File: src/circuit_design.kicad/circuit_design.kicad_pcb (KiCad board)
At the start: 2 copper layers, 198.8 x 170.8 mm, 186 parts, among them J1 CONN_BAT, Q1 BT134-600E, Q2 BT134-600E, Q3 BT134-600E, Q4 BT134-600E, U1 К176ИЕ12, U10 К155ЛА4, U11 К155ЛИ1, U12 К155ЛА1, U13 К155ИЕ5, U14 К155ЛЛ1, U15 К155ЛН1, U16 К155ЛИ1, U17 К155ТВ15, U18 К155ИЕ5, U19 К155ЛП5, U2 К155ЛП10, U20 К155ИВ1, U21 К155ИД7, U22 К155ИД4, U23 К155ЛН1, U24 К155ЛП10, U25 MOC3062M, U26 MOC3062M, U27 MOC3062M, U28 MOC3062M, U29 LM7806_TO220, U3 К155ЛЕ3, U30 SC6038, U31 К155ЛЕ1, U32 К155ЛН1, U33 К155ЛИ1, U34 К155ЛА4, U35 К155ТВ15, U36 К155ТЛ2, U37 4020, U38 LM7806_TO220, U39 К155ЛН1, U4 К155ЛН1, U5 К155ЛИ1, U6 К155ЛЛ1, U7 4020, U8 ICL7660, U9 К155ИЕ5, Y1 32768

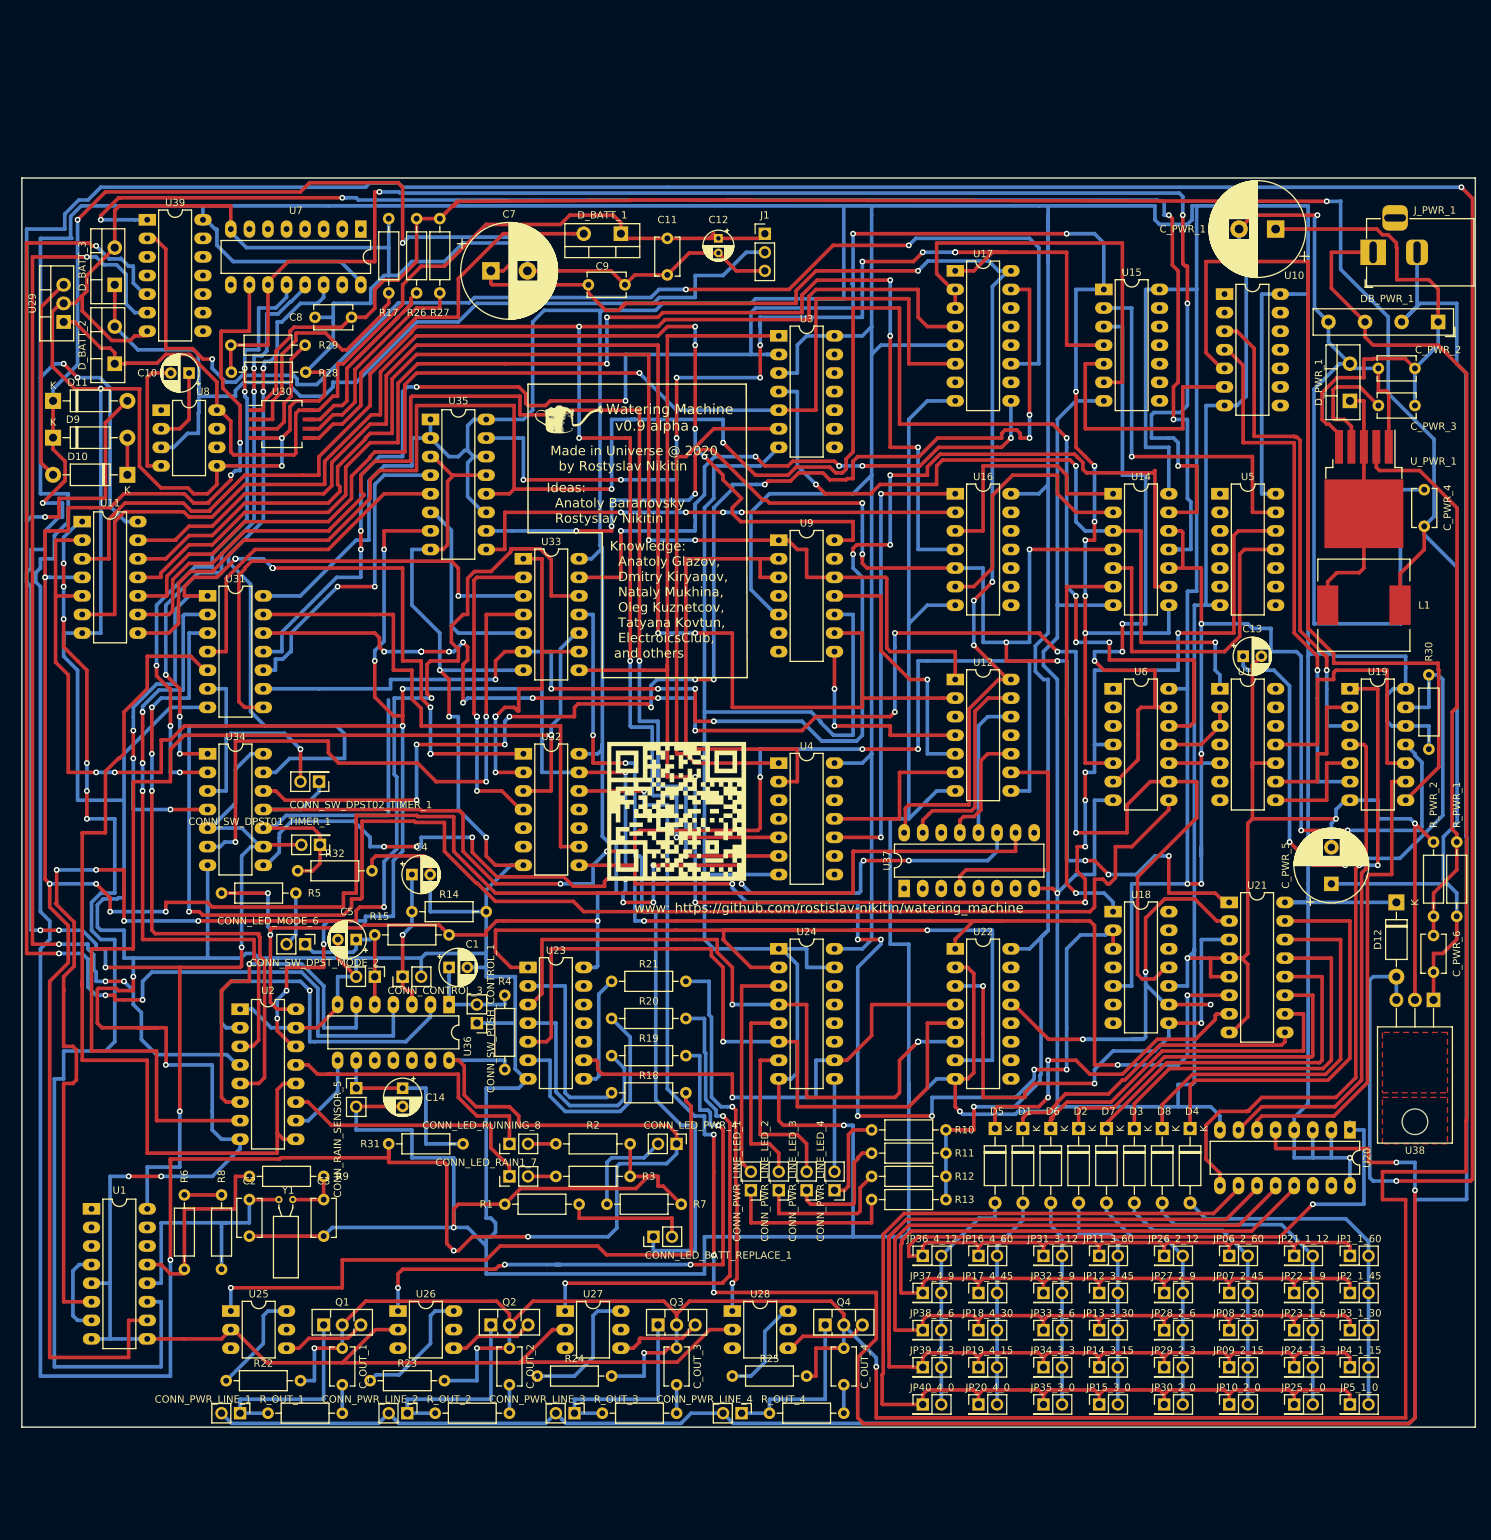
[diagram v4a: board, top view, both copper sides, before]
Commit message: 01. The power module was moved bottom 02. The zone time select jumpers was replaced with sliding switches 03. The zone time select module was moved top 04. The 24-hour timer LED circuit was added
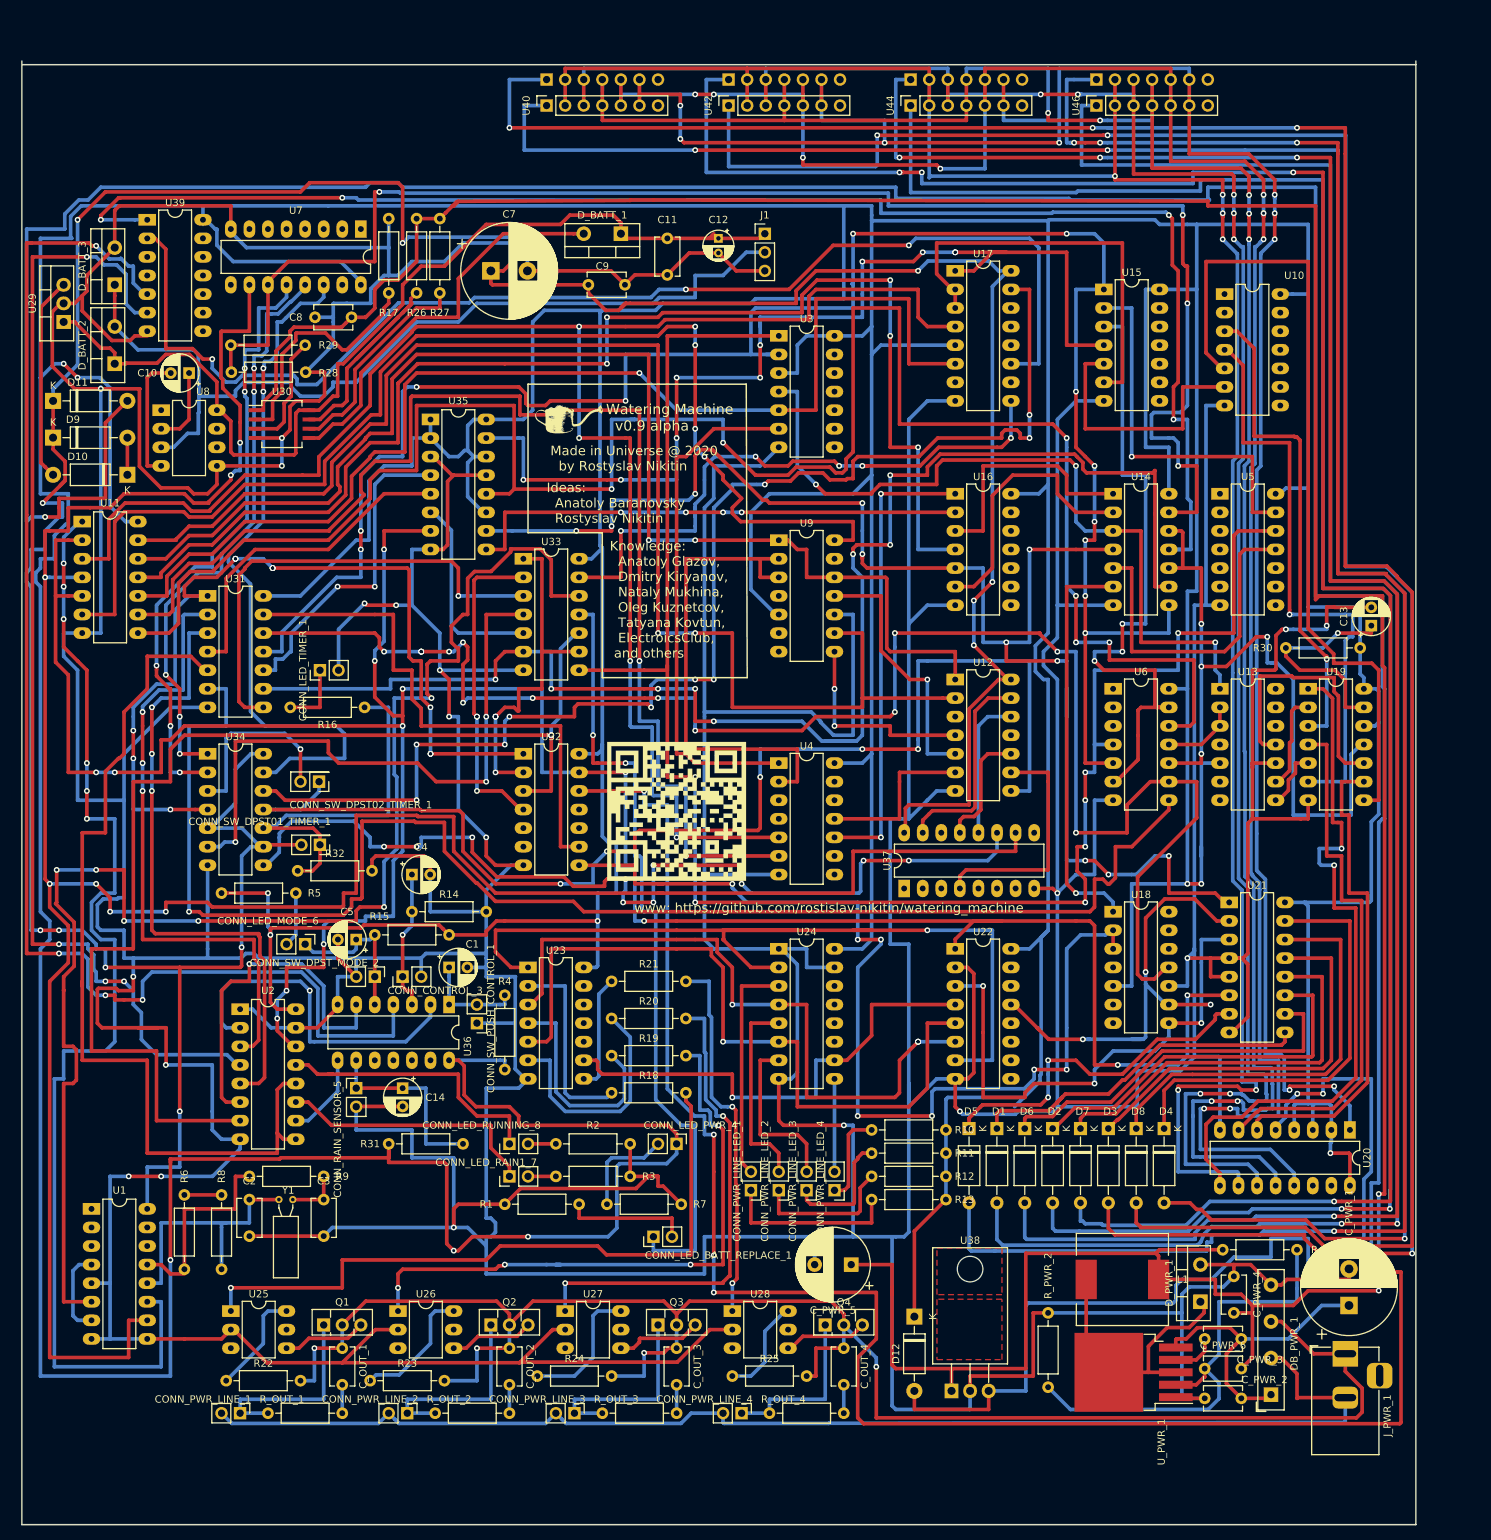
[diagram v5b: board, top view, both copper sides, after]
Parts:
- removed JP06_2_60, JP07_2_45, JP08_2_30, JP09_2_15, JP10_2_0, JP11_3_60, JP12_3_45, JP13_3_30, JP14_3_15, JP15_3_0, JP16_4_60, JP17_4_45, JP18_4_30, JP19_4_15, JP1_1_60, JP20_4_0, JP21_1_12, JP22_1_9, JP23_1_6, JP24_1_3, JP25_1_0, JP26_2_12, JP27_2_9, JP28_2_6, JP29_2_3, JP2_1_45, JP30_2_0, JP31_3_12, JP32_3_9, JP33_3_6, JP34_3_3, JP35_3_0, JP36_4_12, JP37_4_9, JP38_4_6, JP39_4_3, JP3_1_30, JP40_4_0, JP4_1_15, JP5_1_0: JP, Connector_PinHeader_2.54mm:PinHeader_2x01_P2.54mm_Vertical
- added CONN_LED_TIMER_1: Conn_01x02_Male, Connector_PinHeader_2.54mm:PinHeader_1x02_P2.54mm_Vertical, F.Cu at (90.9, 76.2)
- added R16: 270, Resistor_THT:R_Axial_DIN0207_L6.3mm_D2.5mm_P10.16mm_Horizontal, F.Cu at (97.0, 81.3)
- added U40: SPFT_Sliding_Switch, Connector_PinSocket_2.54mm:PinSocket_1x07_P2.54mm_Vertical, F.Cu at (121.9, -1.02)
- added U41: SPFT_Sliding_Switch, Connector_PinSocket_2.54mm:PinSocket_1x07_P2.54mm_Vertical, B.Cu at (121.9, -4.57)
- added U42: SPFT_Sliding_Switch, Connector_PinSocket_2.54mm:PinSocket_1x07_P2.54mm_Vertical, F.Cu at (146.8, -1.02)
- added U43: SPFT_Sliding_Switch, Connector_PinSocket_2.54mm:PinSocket_1x07_P2.54mm_Vertical, B.Cu at (146.8, -4.57)
- added U44: SPFT_Sliding_Switch, Connector_PinSocket_2.54mm:PinSocket_1x07_P2.54mm_Vertical, F.Cu at (171.7, -1.02)
- added U45: SPFT_Sliding_Switch, Connector_PinSocket_2.54mm:PinSocket_1x07_P2.54mm_Vertical, B.Cu at (171.7, -4.57)
- added U46: SPFT_Sliding_Switch, Connector_PinSocket_2.54mm:PinSocket_1x07_P2.54mm_Vertical, F.Cu at (197.1, -1.02)
- added U47: SPFT_Sliding_Switch, Connector_PinSocket_2.54mm:PinSocket_1x07_P2.54mm_Vertical, B.Cu at (197.1, -4.57)
- moved J_PWR_1 150.7 mm to (231.1, 169.7), turned to 90 degrees
- moved DB_PWR_1 148.5 mm to (221.0, 175.3), turned to 90 degrees
- moved C_PWR_1 147.5 mm to (231.6, 163.1), turned to 90 degrees
- moved C_PWR_2 142.8 mm to (216.9, 175.8)
- moved C_PWR_3 129.8 mm to (216.9, 167.6)
- moved D_PWR_1 124.9 mm to (211.3, 162.6)
- moved U_PWR_1 124.8 mm to (202.2, 172.2), turned to 180 degrees
- moved C_PWR_4 110.7 mm to (215.9, 164.1)
- moved L1 97.9 mm to (200.7, 159.5)
- moved D12 86.9 mm to (172.2, 164.6)
- moved U38 84.9 mm to (177.3, 174.8), turned to 0 degrees
- moved C_PWR_5 83.8 mm to (163.6, 157.5), turned to 180 degrees
- moved R_PWR_2 83.2 mm to (190.5, 174.2)
- moved C_PWR_6 60.3 mm to (216.9, 171.7), turned to 180 degrees
- moved R_PWR_1 55.7 mm to (214.4, 155.4), turned to 0 degrees
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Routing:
- net Net-(D8-Pad2): track 44.7 -> 328.3 mm, vias 0 -> 3
- net Net-(D7-Pad2): track 34.5 -> 299.9 mm, vias 0 -> 4
- net Net-(D3-Pad2): track 39.6 -> 303.5 mm, vias 0 -> 3
- net Net-(D4-Pad2): track 48.9 -> 311.7 mm, vias 0 -> 3
- net Net-(D6-Pad2): track 28.2 -> 282.6 mm, vias 0 -> 4
- net Net-(D5-Pad2): track 31.9 -> 275.7 mm, vias 0 -> 4
- net Net-(D2-Pad2): track 32.3 -> 270.3 mm, vias 0 -> 2
- net Net-(D1-Pad2): track 29.0 -> 258.6 mm, vias 0 -> 2
- net VAC: track 415.7 -> 238.4 mm
- net GNDREF: track 346.5 -> 176.3 mm
- net /D3: track 140.1 -> 301.8 mm, vias 0 -> 9
- net /D2: track 144.4 -> 295.7 mm, vias 0 -> 7
- net /D4: track 153.4 -> 296.6 mm, vias 1 -> 9
- net +9V: track 320.6 -> 460.1 mm, vias 1 -> 2
- net /D0: track 153.3 -> 290.9 mm, vias 0 -> 6
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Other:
- board size 198.8 x 170.8 mm -> 190.6 x 200.2 mm

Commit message: The PCB was updated to be compartible with KRADEX Z26 box   01. Connectors was replaced with buttons, LEDs and terminal blocks   02. Buttons, LEDs and terminal blocks positioning was updated Out finish signal was added Other elements positions was updated Dimensions was updated
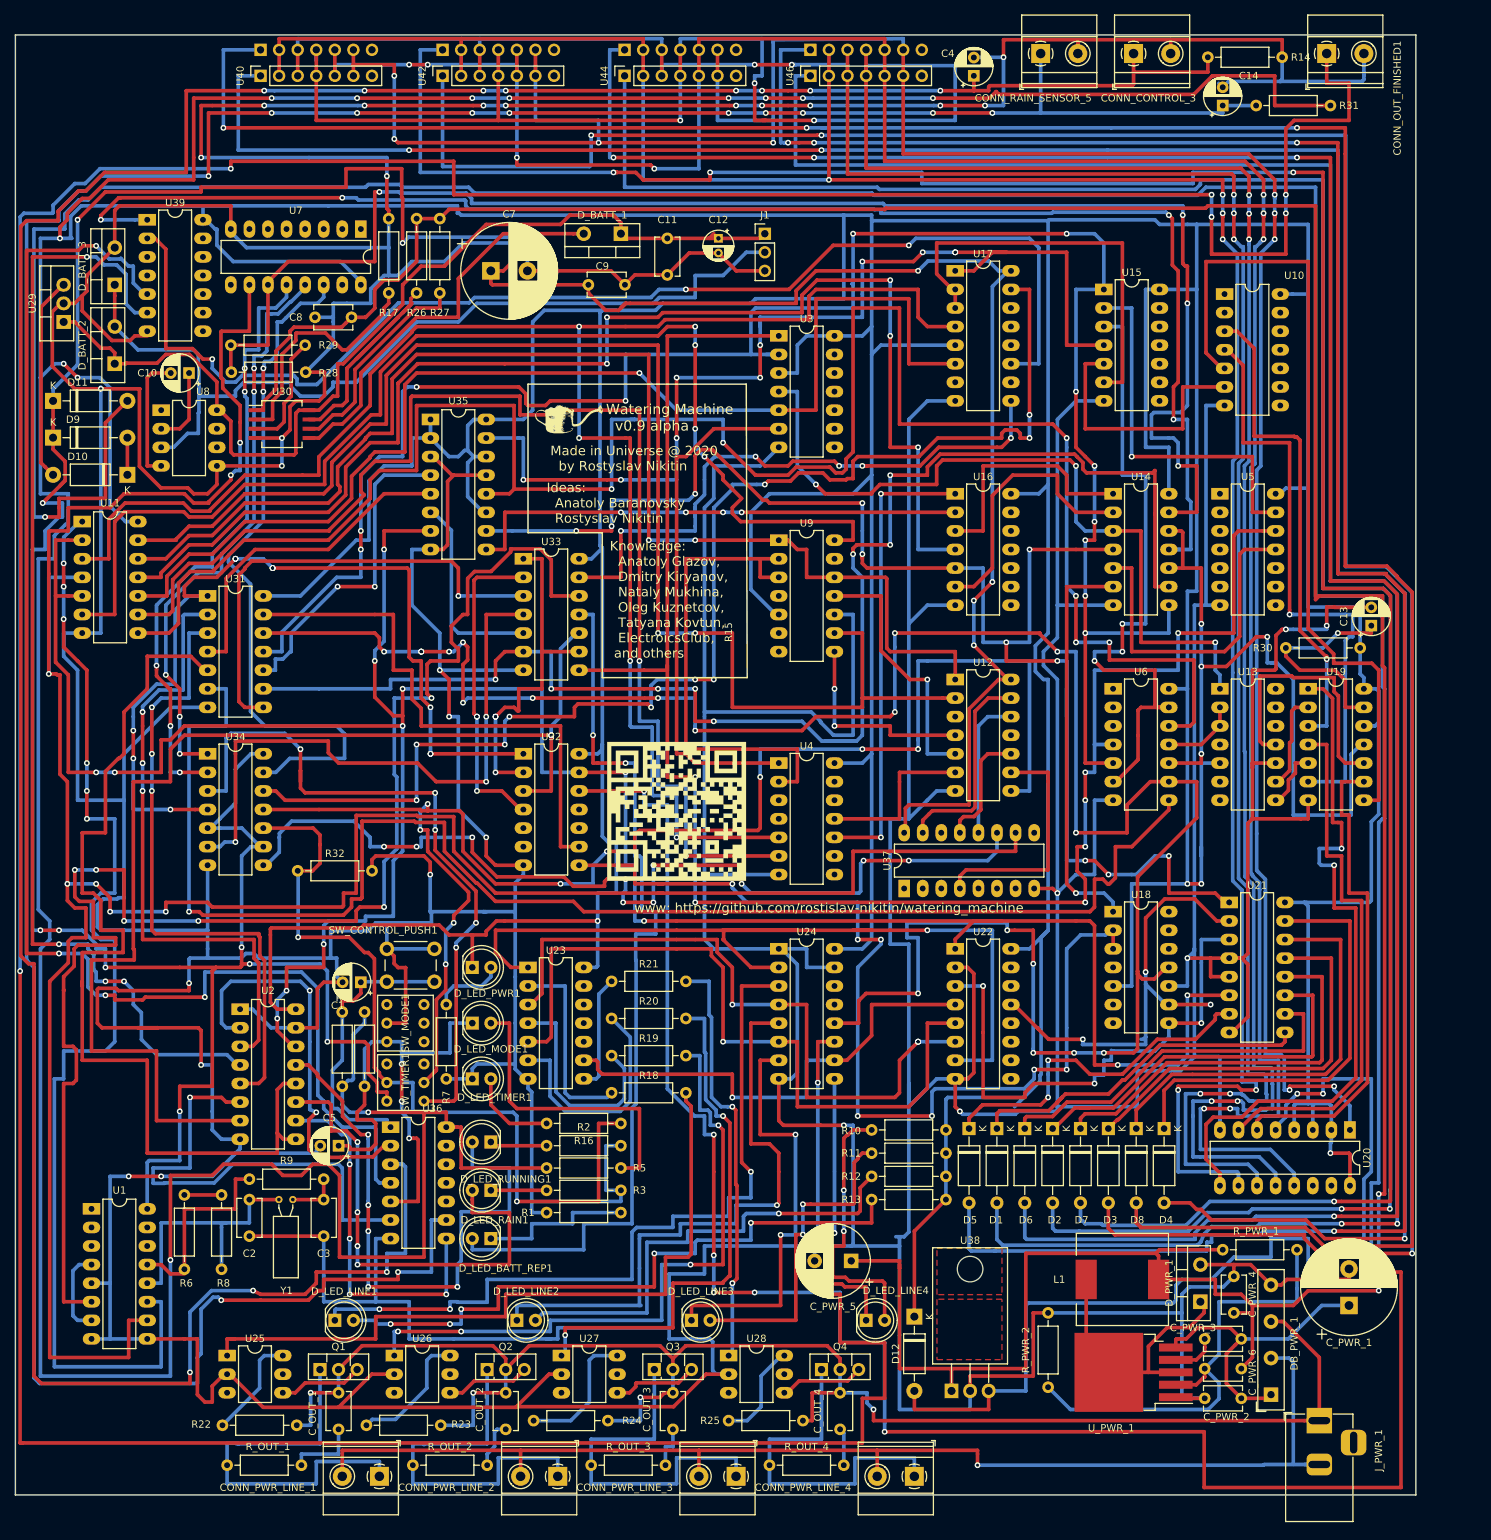
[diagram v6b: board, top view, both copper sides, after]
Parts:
- removed CONN_LED_BATT_REPLACE_1, CONN_LED_MODE_6, CONN_LED_PWR_4, CONN_LED_RAIN1_7, CONN_LED_RUNNING_8, CONN_LED_TIMER_1, CONN_PWR_LINE_LED_1, CONN_PWR_LINE_LED_2, CONN_PWR_LINE_LED_3, CONN_PWR_LINE_LED_4, CONN_SW_DPST_MODE_2, CONN_SW_PUSH_CONTROL_1: Conn_01x02_Male, Connector_PinHeader_2.54mm:PinHeader_1x02_P2.54mm_Vertical
- removed CONN_SW_DPST01_TIMER_1, CONN_SW_DPST02_TIMER_1: Conn_01x02_Male, Connector_PinHeader_2.54mm:PinHeader_2x01_P2.54mm_Vertical
- added CONN_OUT_FINISHED1: Conn_01x02_Male, TerminalBlock_Phoenix:TerminalBlock_Phoenix_MKDS-1,5-2-5.08_1x02_P5.08mm_Horizontal, F.Cu at (228.6, -8.13)
- added D_LED_BATT_REP1: LED, LED_THT:LED_D5.0mm, F.Cu at (114.3, 153.9)
- added D_LED_LINE1: LED, LED_THT:LED_D5.0mm, F.Cu at (93.0, 165.1)
- added D_LED_LINE2: LED, LED_THT:LED_D5.0mm, F.Cu at (117.9, 165.1)
- added D_LED_LINE3: LED, LED_THT:LED_D5.0mm, F.Cu at (141.7, 165.1)
- added D_LED_LINE4: LED, LED_THT:LED_D5.0mm, F.Cu at (165.6, 165.1)
- added D_LED_MODE1: LED, LED_THT:LED_D5.0mm, F.Cu at (111.8, 124.5)
- added D_LED_PWR1: LED, LED_THT:LED_D5.0mm, F.Cu at (111.8, 116.8)
- added D_LED_RAIN1: LED, LED_THT:LED_D5.0mm, F.Cu at (114.3, 147.3)
- added D_LED_RUNNING1: LED, LED_THT:LED_D5.0mm, F.Cu at (114.3, 140.7)
- added D_LED_TIMER1: LED, LED_THT:LED_D5.0mm, F.Cu at (111.8, 132.1)
- added SW_CONTROL_PUSH1: SW_DPST_x2, Button_Switch_THT:SW_PUSH_6mm, F.Cu at (100.1, 114.3)
- added SW_MODE1: SW_DPDT_x2, circuit_design:PB22E09, F.Cu at (102.6, 119.4)
- added SW_TIMER1: SW_DPDT_x2, circuit_design:PB22E09, F.Cu at (102.6, 127.5)
- CONN_CONTROL_3, CONN_PWR_LINE_1, CONN_PWR_LINE_2, CONN_PWR_LINE_3, CONN_PWR_LINE_4, CONN_RAIN_SENSOR_5: footprint Connector_PinHeader_2.54mm:PinHeader_1x02_P2.54mm_Vertical -> TerminalBlock_Phoenix:TerminalBlock_Phoenix_MKDS-1,5-2-5.08_1x02_P5.08mm_Horizontal
- moved R31 191.7 mm to (229.1, -1.02), turned to 180 degrees
- moved C14 175.0 mm to (214.4, -1.02), turned to 90 degrees
- moved CONN_RAIN_SENSOR_5 169.6 mm to (189.5, -8.13)
- moved CONN_CONTROL_3 161.0 mm to (202.2, -8.13), turned to 0 degrees
- moved R14 159.7 mm to (212.3, -7.62)
- moved C4 133.5 mm to (180.3, -5.08), turned to 90 degrees
- moved R16 66.8 mm to (132.1, 138.2)
- moved R5 58.2 mm to (121.9, 144.3)
- moved U42 39.3 mm to (107.7, -5.08)
- moved U43 39.3 mm to (107.7, -8.64)
- moved U44 39.3 mm to (132.6, -5.08)
- moved U45 39.3 mm to (132.6, -8.64)
- moved U46 39.3 mm to (158.0, -5.08)
- moved U47 39.3 mm to (158.0, -8.64)
- moved U40 39.3 mm to (82.8, -5.08)
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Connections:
- U18 pad 11: Net-(U18-Pad11) -> Finished
- U24 pad 12: Net-(U24-Pad12) -> Finished
- U31 pad 12: Net-(U18-Pad11) -> Finished
- U6 pad 9: Net-(U18-Pad11) -> Finished
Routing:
- net Net-(CONN_OUT_FINISHED1-Pad1): track 0.00 -> 583.3 mm, vias 0 -> 8
- net /Conn_Control_Raw: track 19.9 -> 427.7 mm, vias 1 -> 11
- net /Rain_Sensor_Raw: track 26.0 -> 428.6 mm, vias 0 -> 12
- net Finished: track 0.00 -> 308.6 mm, vias 0 -> 20
- net GND: track 1959.9 -> 2195.9 mm, vias 19 -> 29
- net Net-(U18-Pad11): track 222.3 -> 0.00 mm, vias 14 -> 0
- net +5V: track 1626.5 -> 1784.4 mm, vias 11 -> 17
- net /D2: track 295.7 -> 388.8 mm, vias 7 -> 8
- net Net-(D_LED_LINE1-Pad1): track 31.0 -> 107.9 mm, vias 0 -> 3
- net Net-(SW_TIMER1-Pad6): track 25.5 -> 96.4 mm, vias 1 -> 5
- net Net-(D_LED_LINE1-Pad2): track 24.1 -> 88.2 mm, vias 0 -> 5
- net Net-(R16-Pad1): track 51.3 -> 113.0 mm, vias 0 -> 2
- net /D4: track 296.6 -> 356.0 mm
- net Net-(D_LED_LINE2-Pad1): track 27.2 -> 83.4 mm, vias 0 -> 1
- net /D3: track 301.8 -> 353.6 mm
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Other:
- board size 190.6 x 200.2 mm -> 191.5 x 199.6 mm
